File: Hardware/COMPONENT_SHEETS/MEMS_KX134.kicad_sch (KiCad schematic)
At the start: 2 parts, among them U2 KX134-1211

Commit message: Corrected PCB edge cuts, removed components
Will be mimicking layout done by Seth Sievers
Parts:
- renumbered C23 to C13, U2 to U8
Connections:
- net GND: no longer U8.1 (SDO/ADDR)
- new net ADDR: U8.1 (SDO/ADDR)
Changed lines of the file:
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@@
-    (stroke (width 0) (type default) (color 0 0 0 0))
-  )
-  (wire (pts (xy 132.08 87.63) (xy 132.08 91.44))
     (stroke (width 0) (type default) (color 0 0 0 0))
   )
@@
   )
   (polyline (pts (xy 116.84 64.77) (xy 116.84 107.95))
-    (stroke (width 0) (type default) (color 0 0 0 0))
-  )
-  (wire (pts (xy 140.97 87.63) (xy 132.08 87.63))
     (stroke (width 0) (type default) (color 0 0 0 0))
   )
@@
     (effects (font (size 2.54 2.54)) (justify right bottom))
   )
+  (hierarchical_label "ADDR" (shape input) (at 140.97 87.63 180)
+    (effects (font (size 1.27 1.27)) (justify right))
+  )
   (hierarchical_label "SCL" (shape bidirectional) (at 140.97 90.17 180)
     (effects (font (size 1.27 1.27)) (justify right))
@@
   (symbol (lib_id "Data_Collection_KiCAD_Project-rescue:KX122-1042-Sensor_Motion-Data_Collection_KiCAD_Project-rescue") (at 151.13 87.63 0) (unit 1)
     (in_bom yes) (on_board yes)
-    (property "Reference" "U2" (id 0) (at 151.13 66.04 0))
+    (property "Reference" "U8" (id 0) (at 151.13 66.04 0))
     (property "Value" "KX134-1211" (id 1) (at 151.13 68.58 0))
     (property "Footprint" "Package_LGA:LGA-12_2x2mm_P0.5mm" (id 2) (at 154.94 73.66 0)
@@
   (symbol (lib_id "Data_Collection_KiCAD_Project-rescue:GND-power-Data_Collection_KiCAD_Project-rescue") (at 151.13 100.33 0) (unit 1)
     (in_bom yes) (on_board yes)
-    (property "Reference" "#PWR0107" (id 0) (at 151.13 106.68 0)
+    (property "Reference" "#PWR044" (id 0) (at 151.13 106.68 0)
       (effects (font (size 1.27 1.27)) hide)
     )
@@
   (symbol (lib_id "Data_Collection_KiCAD_Project-rescue:+3.3V-power-Data_Collection_KiCAD_Project-rescue") (at 135.89 73.66 0) (unit 1)
     (in_bom yes) (on_board yes)
-    (property "Reference" "#PWR0108" (id 0) (at 135.89 77.47 0)
+    (property "Reference" "#PWR043" (id 0) (at 135.89 77.47 0)
       (effects (font (size 1.27 1.27)) hide)
     )
@@
   (symbol (lib_id "Data_Collection_KiCAD_Project-rescue:C_Small-Device-Data_Collection_KiCAD_Project-rescue") (at 163.83 73.66 270) (unit 1)
     (in_bom yes) (on_board yes)
-    (property "Reference" "C23" (id 0) (at 163.83 67.8434 90))
+    (property "Reference" "C13" (id 0) (at 163.83 67.8434 90))
     (property "Value" "0.1uF" (id 1) (at 163.83 70.1548 90))
     (property "Footprint" "Capacitor_SMD:C_0603_1608Metric_Pad1.08x0.95mm_HandSolder" (id 2) (at 163.83 73.66 0)
@@
   (symbol (lib_id "Data_Collection_KiCAD_Project-rescue:GND-power-Data_Collection_KiCAD_Project-rescue") (at 168.91 73.66 0) (unit 1)
     (in_bom yes) (on_board yes)
-    (property "Reference" "#PWR0109" (id 0) (at 168.91 80.01 0)
+    (property "Reference" "#PWR045" (id 0) (at 168.91 80.01 0)
       (effects (font (size 1.27 1.27)) hide)
     )
@@
     (pin "1")
   )
-  (symbol (lib_id "Data_Collection_KiCAD_Project-rescue:GND-power-Data_Collection_KiCAD_Project-rescue") (at 132.08 91.44 0) (unit 1)
+  (symbol (lib_id "Data_Collection_KiCAD_Project-rescue:GND-power-Data_Collection_KiCAD_Project-rescue") (at 170.18 99.06 0) (unit 1)
     (in_bom yes) (on_board yes)
-    (property "Reference" "#PWR0110" (id 0) (at 132.08 97.79 0)
+    (property "Reference" "#PWR046" (id 0) (at 170.18 105.41 0)
       (effects (font (size 1.27 1.27)) hide)
     )
-    (property "Value" "GND" (id 1) (at 132.207 95.8342 0))
-    (property "Footprint" "" (id 2) (at 132.08 91.44 0)
-      (effects (font (size 1.27 1.27)) hide)
-    )
-    (property "Datasheet" "" (id 3) (at 132.08 91.44 0)
-      (effects (font (size 1.27 1.27)) hide)
-    )
-    (pin "1")
-  )
-  (symbol (lib_id "Data_Collection_KiCAD_Project-rescue:GND-power-Data_Collection_KiCAD_Project-rescue") (at 170.18 99.06 0) (unit 1)
-    (in_bom yes) (on_board yes)
-    (property "Reference" "#PWR0111" (id 0) (at 170.18 105.41 0)
-      (effects (font (size 1.27 1.27)) hide)
-    )

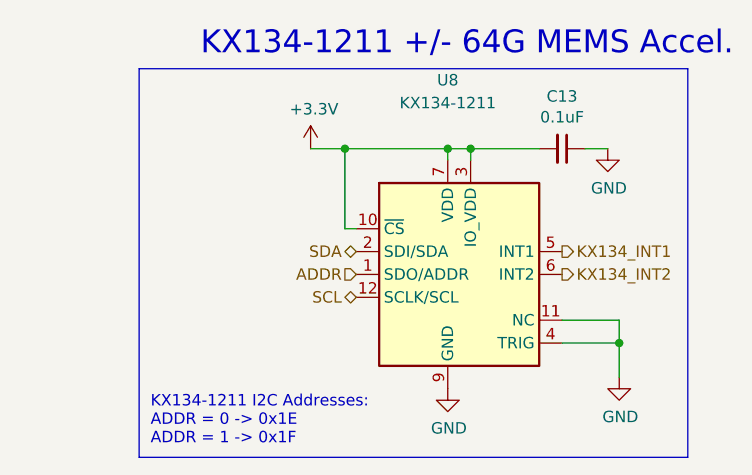
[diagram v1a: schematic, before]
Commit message: Organized components, arranged filter caps
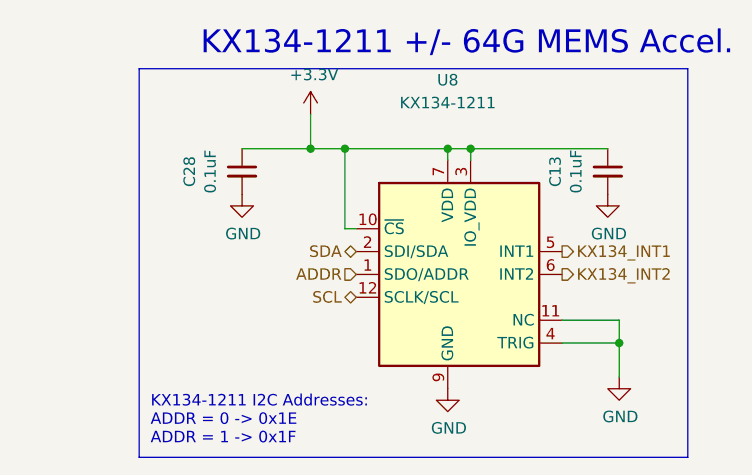
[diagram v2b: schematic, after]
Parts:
- added C28: 0.1uF, Capacitor_SMD:C_0603_1608Metric_Pad1.08x0.95mm_HandSolder, symbol Data_Collection_KiCAD_Project-rescue:C_Small-Device-Data_Collection_KiCAD_Proje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
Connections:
- net +3V3: now also C13.1, C28.1; no longer C13.2
- net GND: now also C13.2, C28.2; no longer C13.1
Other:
- moved on the sheet: C13
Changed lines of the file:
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@@
   (junction (at 153.67 73.66) (diameter 0) (color 0 0 0 0)
   )
+  (junction (at 135.89 73.66) (diameter 0) (color 0 0 0 0)
+  )
   (junction (at 139.7 73.66) (diameter 0) (color 0 0 0 0)
   )
@@
     (stroke (width 0) (type default) (color 0 0 0 0))
   )
+  (wire (pts (xy 128.27 73.66) (xy 135.89 73.66))
+    (stroke (width 0) (type default) (color 0 0 0 0))
+  )
+  (wire (pts (xy 139.7 82.55) (xy 139.7 73.66))
+    (stroke (width 0) (type default) (color 0 0 0 0))
+  )
+  (wire (pts (xy 153.67 74.93) (xy 153.67 73.66))
+    (stroke (width 0) (type default) (color 0 0 0 0))
+  )
+  (wire (pts (xy 163.83 92.71) (xy 170.18 92.71))
+    (stroke (width 0) (type default) (color 0 0 0 0))
+  )
   (wire (pts (xy 135.89 73.66) (xy 139.7 73.66))
     (stroke (width 0) (type default) (color 0 0 0 0))
   )
-  (wire (pts (xy 139.7 82.55) (xy 139.7 73.66))
-    (stroke (width 0) (type default) (color 0 0 0 0))
-  )
-  (wire (pts (xy 153.67 74.93) (xy 153.67 73.66))
-    (stroke (width 0) (type default) (color 0 0 0 0))
-  )
-  (wire (pts (xy 163.83 92.71) (xy 170.18 92.71))
-    (stroke (width 0) (type default) (color 0 0 0 0))
-  )
   (wire (pts (xy 151.13 73.66) (xy 153.67 73.66))
     (stroke (width 0) (type default) (color 0 0 0 0))
   )
-  (wire (pts (xy 153.67 73.66) (xy 161.29 73.66))
+  (wire (pts (xy 153.67 73.66) (xy 168.91 73.66))
     (stroke (width 0) (type default) (color 0 0 0 0))
   )
@@
     (stroke (width 0) (type default) (color 0 0 0 0))
   )
+  (wire (pts (xy 135.89 69.85) (xy 135.89 73.66))
+    (stroke (width 0) (type default) (color 0 0 0 0))
+  )
   (polyline (pts (xy 116.84 64.77) (xy 116.84 107.95))
     (stroke (width 0) (type default) (color 0 0 0 0))
@@
   )
   (wire (pts (xy 170.18 92.71) (xy 170.18 95.25))
-    (stroke (width 0) (type default) (color 0 0 0 0))
-  )
-  (wire (pts (xy 166.37 73.66) (xy 168.91 73.66))
     (stroke (width 0) (type default) (color 0 0 0 0))
   )
@@
     (pin "1")
   )
-  (symbol (lib_id "Data_Collection_KiCAD_Project-rescue:+3.3V-power-Data_Collection_KiCAD_Project-rescue") (at 135.89 73.66 0) (unit 1)
-    (in_bom yes) (on_board yes)
-    (property "Reference" "#PWR043" (id 0) (at 135.89 77.47 0)
-      (effects (font (size 1.27 1.27)) hide)
-    )
-    (property "Value" "+3.3V" (id 1) (at 136.271 69.2658 0))
-    (property "Footprint" "" (id 2) (at 135.89 73.66 0)
-      (effects (font (size 1.27 1.27)) hide)
-    )
-    (property "Datasheet" "" (id 3) (at 135.89 73.66 0)
-      (effects (font (size 1.27 1.27)) hide)
-    )
-    (pin "1")
-  )
-  (symbol (lib_id "Data_Collection_KiCAD_Project-rescue:C_Small-Device-Data_Collection_KiCAD_Project-rescue") (at 163.83 73.66 270) (unit 1)
-    (in_bom yes) (on_board yes)
-    (property "Reference" "C13" (id 0) (at 163.83 67.8434 90))
-    (property "Value" "0.1uF" (id 1) (at 163.83 70.1548 90))
-    (property "Footprint" "Capacitor_SMD:C_0603_1608Metric_Pad1.08x0.95mm_HandSolder" (id 2) (at 163.83 73.66 0)
-      (effects (font (size 1.27 1.27)) hide)
-    )
-    (property "Datasheet" "~" (id 3) (at 163.83 73.66 0)
+  (symbol (lib_id "Data_Collection_KiCAD_Project-rescue:+3.3V-power-Data_Collection_KiCAD_Project-rescue") (at 135.89 69.85 0) (unit 1)
+    (in_bom yes) (on_board yes)
+    (property "Reference" "#PWR043" (id 0) (at 135.89 73.66 0)
+      (effects (font (size 1.27 1.27)) hide)
+    )
+    (property "Value" "+3.3V" (id 1) (at 136.271 65.4558 0))
+    (property "Footprint" "" (id 2) (at 135.89 69.85 0)
+      (effects (font (size 1.27 1.27)) hide)
+    )
+    (property "Datasheet" "" (id 3) (at 135.89 69.85 0)
+      (effects (font (size 1.27 1.27)) hide)
+    )
+    (pin "1")
+  )
+  (symbol (lib_id "Data_Collection_KiCAD_Project-rescue:C_Small-Device-Data_Collection_KiCAD_Project-rescue") (at 168.91 76.2 0) (unit 1)
+    (in_bom yes) (on_board yes)
+    (property "Reference" "C13" (id 0) (at 163.0934 76.2 90))
+    (property "Value" "0.1uF" (id 1) (at 165.4048 76.2 90))
+    (property "Footprint" "Capacitor_SMD:C_0603_1608Metric_Pad1.08x0.95mm_HandSolder" (id 2) (at 168.91 76.2 0)
+      (effects (font (size 1.27 1.27)) hide)
+    )
+    (property "Datasheet" "~" (id 3) (at 168.91 76.2 0)
       (effects (font (size 1.27 1.27)) hide)
     )
@@
     (pin "2")
   )
-  (symbol (lib_id "Data_Collection_KiCAD_Project-rescue:GND-power-Data_Collection_KiCAD_Project-rescue") (at 168.91 73.66 0) (unit 1)
-    (in_bom yes) (on_board yes)
-    (property "Reference" "#PWR045" (id 0) (at 168.91 80.01 0)
-      (effects (font (size 1.27 1.27)) hide)
-    )
-    (property "Value" "GND" (id 1) (at 169.037 78.0542 0))
-    (property "Footprint" "" (id 2) (at 168.91 73.66 0)
-      (effects (font (size 1.27 1.27)) hide)
-    )
-    (property "Datasheet" "" (id 3) (at 168.91 73.66 0)
+  (symbol (lib_id "Data_Collection_KiCAD_Project-rescue:GND-power-Data_Collection_KiCAD_Project-rescue") (at 168.91 78.74 0) (unit 1)
+    (in_bom yes) (on_board yes)
+    (property "Reference" "#PWR045" (id 0) (at 168.91 85.09 0)
+      (effects (font (size 1.27 1.27)) hide)
+    )
+    (property "Value" "GND" (id 1) (at 169.037 83.1342 0))
+    (property "Footprint" "" (id 2) (at 168.91 78.74 0)
+      (effects (font (size 1.27 1.27)) hide)
+    )
+    (property "Datasheet" "" (id 3) (at 168.91 78.74 0)
       (effects (font (size 1.27 1.27)) hide)
     )
@@
       (effects (font (size 1.27 1.27)) hide)
     )
+    (pin "1")
+  )
+  (symbol (lib_id "Data_Collection_KiCAD_Project-rescue:C_Small-Device-Data_Collection_KiCAD_Project-rescue") (at 128.27 76.2 0) (unit 1)
+    (in_bom yes) (on_board yes)
+    (property "Reference" "C28" (id 0) (at 122.4534 76.2 90))
+    (property "Value" "0.1uF" (id 1) (at 124.7648 76.2 90))
+    (property "Footprint" "Capacitor_SMD:C_0603_1608Metric_Pad1.08x0.95mm_HandSolder" (id 2) (at 128.27 76.2 0)
+      (effects (font (size 1.27 1.27)) hide)
+    )
+    (property "Datasheet" "~" (id 3) (at 128.27 76.2 0)
+      (effects (font (size 1.27 1.27)) hide)
+    )
+    (pin "1")
+    (pin "2")
+  )
+  (symbol (lib_id "Data_Collection_KiCAD_Project-rescue:GND-power-Data_Collection_KiCAD_Project-rescue") (at 128.27 78.74 0) (unit 1)
+    (in_bom yes) (on_board yes)
+    (property "Reference" "#PWR063" (id 0) (at 128.27 85.09 0)
+      (effects (font (size 1.27 1.27)) hide)
+    )
+    (property "Value" "GND" (id 1) (at 128.397 83.1342 0))
+    (property "Footprint" "" (id 2) (at 128.27 78.74 0)
+      (effects (font (size 1.27 1.27)) hide)
+    )
+    (property "Datasheet" "" (id 3) (at 128.27 78.74 0)
+      (effects (font (size 1.27 1.27)) hide)
+    )
